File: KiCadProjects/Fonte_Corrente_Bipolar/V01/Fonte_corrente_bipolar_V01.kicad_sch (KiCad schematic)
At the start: 48 parts, among them J1 alimentacao analogica, J2 sinais analogicos, J3 comunicacao / sinais digitais, J4 signal select 1, J5 signal select 2, J7 Vref, U1 INA128, U1-howland1 AD828AN, U2 INA128, U3-cond1 AD828AN

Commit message: Baseado barramento v04 - Finalizado
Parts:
- J4: value signal select 1 -> SinA | Sin1
- J5: value signal select 2 -> SinB | Sin2
- J7: value Vref -> +3.3V | +5.0V
- renumbered D5 to L1:+9v1, D6 to L2:-9v1, D7 to L3:+5v1, D8 to L4:+3.3v1, RganhoINA1 to Rganho-I1, RganhoINA2 to Rganho-I2, Rsentinela1 to Rsentinela-I1, Rsentinela2 to Rsentinela-I2, U2 to U1-INA-I1, U1 to U2-INA-I2
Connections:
- net nó1: now also C3.2; no longer C3.1
- net nó2: now also C3.1; no longer C3.2
- net nó3: now also C1.2; no longer C1.1
- net nó4: now also C1.1; no longer C1.2
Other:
- moved on the sheet: C1, C3
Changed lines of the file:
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@@
   (symbol (lib_id "Device:LED") (at 47.625 120.269 90) (unit 1)
     (in_bom yes) (on_board yes) (dnp no) (fields_autoplaced)
-    (property "Reference" "D7" (at 50.8 120.5865 90)
+    (property "Reference" "L3:+5v1" (at 50.8 120.5865 90)
       (effects (font (size 1.27 1.27)) (justify right))
     )
@@
       (project "Fonte_corrente_bipolar_V01"
         (path "/f0ff92cf-26e5-4ab9-977d-5f9689e8a5d0"
-          (reference "D7") (unit 1)
+          (reference "L3:+5v1") (unit 1)
         )
       )
@@
   (symbol (lib_id "Device:R") (at 213.868 64.643 0) (unit 1)
     (in_bom yes) (on_board yes) (dnp no) (fields_autoplaced)
-    (property "Reference" "RganhoINA2" (at 216.408 63.373 0)
-      (effects (font (size 1.27 1.27)) (justify left))
-    )
-    (property "Value" "3,3k" (at 216.408 65.913 0)
+    (property "Reference" "Rganho-I2" (at 215.9 63.373 0)
+      (effects (font (size 1.27 1.27)) (justify left))
+    )
+    (property "Value" "3,3k" (at 215.9 65.913 0)
       (effects (font (size 1.27 1.27)) (justify left))
     )
@@
       (project "Fonte_corrente_bipolar_V01"
         (path "/f0ff92cf-26e5-4ab9-977d-5f9689e8a5d0"
-          (reference "RganhoINA2") (unit 1)
+          (reference "Rganho-I2") (unit 1)
         )
       )
@@
   (symbol (lib_id "Amplifier_Instrumentation:INA128") (at 242.189 36.068 0) (unit 1)
     (in_bom yes) (on_board yes) (dnp no)
-    (property "Reference" "U2" (at 248.793 26.924 0)
+    (property "Reference" "U1-INA-I1" (at 248.793 26.924 0)
       (effects (font (size 1.27 1.27)))
     )
@@
       (project "Fonte_corrente_bipolar_V01"
         (path "/f0ff92cf-26e5-4ab9-977d-5f9689e8a5d0"
-          (reference "U2") (unit 1)
+          (reference "U1-INA-I1") (unit 1)
         )
       )
@@
     )
   )
-  (symbol (lib_id "Device:C_Polarized_Small_US") (at 238.252 131.572 90) (unit 1)
-    (in_bom yes) (on_board yes) (dnp no) (fields_autoplaced)
-    (property "Reference" "C3" (at 237.8202 125.857 90)
-      (effects (font (size 1.27 1.27)))
-    )
-    (property "Value" "1 uF" (at 237.8202 128.397 90)
+  (symbol (lib_id "Device:C_Polarized_Small_US") (at 238.252 131.572 270) (mirror x) (unit 1)
+    (in_bom yes) (on_board yes) (dnp no)
+    (property "Reference" "C3" (at 238.6838 125.857 90)
+      (effects (font (size 1.27 1.27)))
+    )
+    (property "Value" "1 uF" (at 238.6838 128.397 90)
       (effects (font (size 1.27 1.27)))
     )
@@
   (symbol (lib_id "Device:R") (at 226.314 36.068 0) (unit 1)
     (in_bom yes) (on_board yes) (dnp no) (fields_autoplaced)
-    (property "Reference" "RganhoINA1" (at 228.854 34.798 0)
-      (effects (font (size 1.27 1.27)) (justify left))
-    )
-    (property "Value" "3,3k" (at 228.854 37.338 0)
+    (property "Reference" "Rganho-I1" (at 228.6 34.798 0)
+      (effects (font (size 1.27 1.27)) (justify left))
+    )
+    (property "Value" "3,3k" (at 228.6 37.338 0)
       (effects (font (size 1.27 1.27)) (justify left))
     )
@@
       (project "Fonte_corrente_bipolar_V01"
         (path "/f0ff92cf-26e5-4ab9-977d-5f9689e8a5d0"
-          (reference "RganhoINA1") (unit 1)
+          (reference "Rganho-I1") (unit 1)
         )
       )
@@
   (symbol (lib_id "Device:R") (at 214.249 36.068 0) (unit 1)
     (in_bom yes) (on_board yes) (dnp no) (fields_autoplaced)
-    (property "Reference" "Rsentinela1" (at 216.154 34.798 0)
-      (effects (font (size 1.27 1.27)) (justify left))
-    )
-    (property "Value" "10" (at 216.154 37.338 0)
+    (property "Reference" "Rsentinela-I1" (at 217.17 34.798 0)
+      (effects (font (size 1.27 1.27)) (justify left))
+    )
+    (property "Value" "10" (at 217.17 37.338 0)
       (effects (font (size 1.27 1.27)) (justify left))
     )
@@
       (project "Fonte_corrente_bipolar_V01"
         (path "/f0ff92cf-26e5-4ab9-977d-5f9689e8a5d0"
-          (reference "Rsentinela1") (unit 1)
+          (reference "Rsentinela-I1") (unit 1)
         )
       )
@@
       (effects (font (size 1.27 1.27)) (justify left) hide)
     )
-    (property "Value" "signal select 2" (at 153.416 61.087 90)
+    (property "Value" "SinB | Sin2" (at 153.416 61.087 90)
       (effects (font (size 1.27 1.27)) (justify right))
     )
@@
   (symbol (lib_id "Device:LED") (at 33.401 120.269 270) (unit 1)
     (in_bom yes) (on_board yes) (dnp no) (fields_autoplaced)
-    (property "Reference" "D6" (at 35.56 117.4115 90)
+    (property "Reference" "L2:-9v1" (at 35.56 117.4115 90)
       (effects (font (size 1.27 1.27)) (justify left))
     )
@@
       (project "Fonte_corrente_bipolar_V01"
         (path "/f0ff92cf-26e5-4ab9-977d-5f9689e8a5d0"
-          (reference "D6") (unit 1)
+          (reference "L2:-9v1") (unit 1)
         )
       )
@@
       (effects (font (size 1.27 1.27)) (justify left) hide)
     )
-    (property "Value" "Vref" (at 201.676 94.234 90)
+    (property "Value" "+3.3V | +5.0V" (at 196.85 93.98 90)
       (effects (font (size 1.27 1.27)) (justify right))
     )
@@
   (symbol (lib_id "Device:LED") (at 62.103 120.269 90) (unit 1)
     (in_bom yes) (on_board yes) (dnp no) (fields_autoplaced)
-    (property "Reference" "D8" (at 66.04 120.5865 90)
+    (property "Reference" "L4:+3.3v1" (at 66.04 120.5865 90)
       (effects (font (size 1.27 1.27)) (justify right))
     )
@@
       (project "Fonte_corrente_bipolar_V01"
         (path "/f0ff92cf-26e5-4ab9-977d-5f9689e8a5d0"
-          (reference "D8") (unit 1)
+          (reference "L4:+3.3v1") (unit 1)
         )
       )
@@
   (symbol (lib_id "Device:LED") (at 18.161 120.396 90) (unit 1)
     (in_bom yes) (on_board yes) (dnp no) (fields_autoplaced)
-    (property "Reference" "D5" (at 21.59 120.7135 90)
+    (property "Reference" "L1:+9v1" (at 21.59 120.7135 90)
       (effects (font (size 1.27 1.27)) (justify right))
     )
@@
       (project "Fonte_corrente_bipolar_V01"
         (path "/f0ff92cf-26e5-4ab9-977d-5f9689e8a5d0"
-          (reference "D5") (unit 1)
+          (reference "L1:+9v1") (unit 1)
         )
       )
@@
   (symbol (lib_id "Amplifier_Instrumentation:INA128") (at 229.743 64.643 0) (unit 1)
     (in_bom yes) (on_board yes) (dnp no)
-    (property "Reference" "U1" (at 236.347 55.499 0)
+    (property "Reference" "U2-INA-I2" (at 236.347 55.499 0)
       (effects (font (size 1.27 1.27)))
     )
@@
       (project "Fonte_corrente_bipolar_V01"
         (path "/f0ff92cf-26e5-4ab9-977d-5f9689e8a5d0"
-          (reference "U1") (unit 1)
+          (reference "U2-INA-I2") (unit 1)
         )
       )
@@
       (effects (font (size 1.27 1.27)) (justify left) hide)
     )
-    (property "Value" "signal select 1" (at 25.908 69.85 90)
+    (property "Value" "SinA | Sin1" (at 27.94 63.5 90)
       (effects (font (size 1.27 1.27)) (justify right))
     )
@@
   (symbol (lib_id "Device:R") (at 201.803 64.643 0) (unit 1)
     (in_bom yes) (on_board yes) (dnp no) (fields_autoplaced)
-    (property "Reference" "Rsentinela2" (at 203.708 63.373 0)
-      (effects (font (size 1.27 1.27)) (justify left))
-    )
-    (property "Value" "10" (at 203.708 65.913 0)
+    (property "Reference" "Rsentinela-I2" (at 204.47 63.373 0)
+      (effects (font (size 1.27 1.27)) (justify left))
+    )
+    (property "Value" "10" (at 204.47 65.913 0)
       (effects (font (size 1.27 1.27)) (justify left))
     )
@@
       (project "Fonte_corrente_bipolar_V01"
         (path "/f0ff92cf-26e5-4ab9-977d-5f9689e8a5d0"
-          (reference "Rsentinela2") (unit 1)
+          (reference "Rsentinela-I2") (unit 1)
         )
       )
@@
     )
   )
-  (symbol (lib_id "Device:C_Polarized_Small_US") (at 167.259 129.54 270) (mirror x) (unit 1)
-    (in_bom yes) (on_board yes) (dnp no) (fields_autoplaced)
-    (property "Reference" "C1" (at 167.6908 123.825 90)
-      (effects (font (size 1.27 1.27)))
-    )
-    (property "Value" "1 uF" (at 167.6908 126.365 90)
-      (effects (font (size 1.27 1.27)))
-    )
+  (symbol (lib_id "Device:C_Polarized_Small_US") (at 167.259 129.54 90) (unit 1)
+    (in_bom yes) (on_board yes) (dnp no)
+    (property "Reference" "C1" (at 166.8272 123.825 90)
+      (effects (font (size 1.27 1.27)))
+    )
+    (property "Value" "1 uF" (at 166.8272 126.365 90)
+      (effects (font (size 1.27 1.27)))
+    )

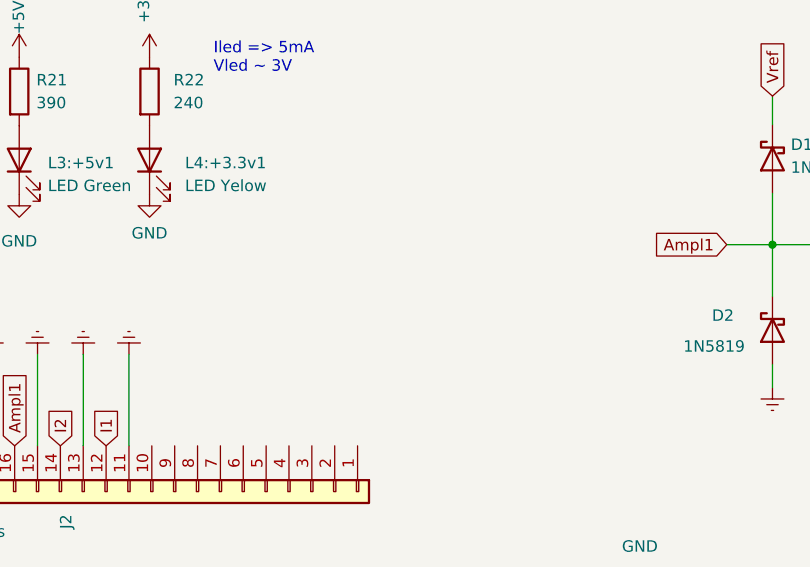
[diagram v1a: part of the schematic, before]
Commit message: Baseado barramento v04 - Finalizado - implementacao resistor pullup i2c 2
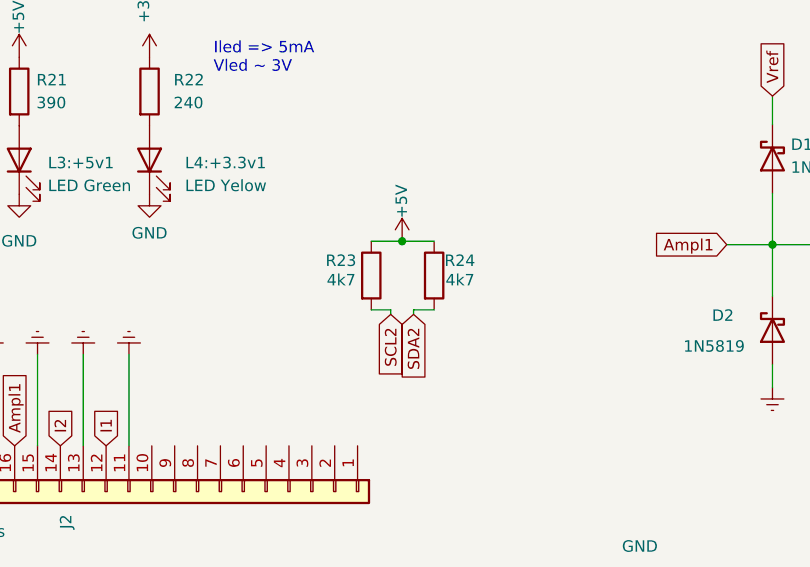
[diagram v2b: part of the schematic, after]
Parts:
- added R23, R24: 4k7, Resistor_THT:R_Axial_DIN0207_L6.3mm_D2.5mm_P7.62mm_Horizontal, symbol Device:R
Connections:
- net +5V: now also R23.1, R24.1
- net SCL2: now also R23.2
- net SDA2: now also R24.2
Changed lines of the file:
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@@
   (junction (at 50.165 40.64) (diameter 0) (color 0 0 0 0)
   )
+  (junction (at 90.17 129.286) (diameter 0) (color 0 0 0 0)
+  )
   (junction (at 120.65 68.58) (diameter 0) (color 0 0 0 0)
   )
@@
     (stroke (width 0) (type default))
   )
+  (wire (pts (xy 91.44 137.414) (xy 91.44 136.906))
+    (stroke (width 0) (type default))
+  )
   (wire (pts (xy 36.5748 177.038) (xy 36.5748 181.864))
     (stroke (width 0) (type default))
@@
     (stroke (width 0) (type default))
   )
+  (wire (pts (xy 93.726 129.286) (xy 90.17 129.286))
+    (stroke (width 0) (type default))
+  )
   (wire (pts (xy 240.792 131.572) (xy 243.332 131.572))
     (stroke (width 0) (type default))
@@
     (stroke (width 0) (type default))
   )
+  (wire (pts (xy 88.9 137.414) (xy 88.9 136.906))
+    (stroke (width 0) (type default))
+  )
   (wire (pts (xy 131.318 129.667) (xy 126.238 129.667))
     (stroke (width 0) (type default))
@@
     (stroke (width 0) (type default))
   )
+  (wire (pts (xy 90.17 129.286) (xy 86.741 129.286))
+    (stroke (width 0) (type default))
+  )
   (wire (pts (xy 25.908 54.737) (xy 22.733 54.737))
     (stroke (width 0) (type default))
@@
     (stroke (width 0) (type default))
   )
+  (wire (pts (xy 88.9 136.906) (xy 86.741 136.906))
+    (stroke (width 0) (type default))
+  )
   (wire (pts (xy 50.165 35.56) (xy 50.165 40.64))
     (stroke (width 0) (type default))
@@
     (stroke (width 0) (type default))
   )
+  (wire (pts (xy 91.44 136.906) (xy 93.726 136.906))
+    (stroke (width 0) (type default))
+  )
   (wire (pts (xy 55.88 86.995) (xy 55.88 83.82))
     (stroke (width 0) (type default))
@@
     )
   )
+  (global_label "SDA2" (shape input) (at 91.44 137.414 270) (fields_autoplaced)
+    (effects (font (size 1.27 1.27)) (justify right))
+    (property "Intersheetrefs" "${INTERSHEET_REFS}" (at 91.44 145.1768 90)
+      (effects (font (size 1.27 1.27)) (justify right) hide)
+    )
+  )
   (global_label "Ampl2" (shape input) (at 274.574 131.699 0) (fields_autoplaced)
     (effects (font (size 1.27 1.27)) (justify left))
@@
     )
   )
+  (global_label "SCL2" (shape input) (at 88.9 137.414 270) (fields_autoplaced)
+    (effects (font (size 1.27 1.27)) (justify right))
+    (property "Intersheetrefs" "${INTERSHEET_REFS}" (at 88.9 145.1163 90)
+      (effects (font (size 1.27 1.27)) (justify right) hide)
+    )
+  )
   (global_label "Vref" (shape input) (at 243.332 115.062 90) (fields_autoplaced)
     (effects (font (size 1.27 1.27)) (justify left))
@@
     )
   )
+  (symbol (lib_id "Device:R") (at 93.726 133.096 0) (unit 1)
+    (in_bom yes) (on_board yes) (dnp no)
+    (property "Reference" "R24" (at 94.869 131.445 0)
+      (effects (font (size 1.27 1.27)) (justify left))
+    )
+    (property "Value" "4k7" (at 94.996 133.604 0)
+      (effects (font (size 1.27 1.27)) (justify left))
+    )
+    (property "Footprint" "Resistor_THT:R_Axial_DIN0207_L6.3mm_D2.5mm_P7.62mm_Horizontal" (at 91.948 133.096 90)
+      (effects (font (size 1.27 1.27)) hide)
+    )
+    (property "Datasheet" "~" (at 93.726 133.096 0)
+      (effects (font (size 1.27 1.27)) hide)
+    )
+    (pin "2")
+    (pin "1")
+    (instances
+      (project "Fonte_corrente_bipolar_V01"
+        (path "/f0ff92cf-26e5-4ab9-977d-5f9689e8a5d0"
+          (reference "R24") (unit 1)
+        )
+      )
+    )
+  )
   (symbol (lib_id "power:Earth") (at 24.257 141.859 180) (unit 1)
     (in_bom yes) (on_board yes) (dnp no) (fields_autoplaced)
@@
     )
   )
+  (symbol (lib_id "Device:R") (at 86.741 133.096 0) (unit 1)
+    (in_bom yes) (on_board yes) (dnp no)
+    (property "Reference" "R23" (at 81.661 131.445 0)
+      (effects (font (size 1.27 1.27)) (justify left))
+    )
+    (property "Value" "4k7" (at 81.788 133.604 0)
+      (effects (font (size 1.27 1.27)) (justify left))
+    )
+    (property "Footprint" "Resistor_THT:R_Axial_DIN0207_L6.3mm_D2.5mm_P7.62mm_Horizontal" (at 84.963 133.096 90)
+      (effects (font (size 1.27 1.27)) hide)
+    )
+    (property "Datasheet" "~" (at 86.741 133.096 0)
+      (effects (font (size 1.27 1.27)) hide)
+    )
+    (pin "1")
+    (pin "2")
+    (instances
+      (project "Fonte_corrente_bipolar_V01"
+        (path "/f0ff92cf-26e5-4ab9-977d-5f9689e8a5d0"
+          (reference "R23") (unit 1)
+        )
+      )
+    )
+  )
   (symbol (lib_id "Device:R") (at 33.401 112.649 0) (unit 1)
     (in_bom yes) (on_board yes) (dnp no) (fields_autoplaced)
@@
         )
       )
+    )
+  )
+  (symbol (lib_id "power:+5V") (at 90.17 129.286 0) (unit 1)
+    (in_bom yes) (on_board yes) (dnp no)
+    (property "Reference" "#PWR061" (at 90.17 133.096 0)
+      (effects (font (size 1.27 1.27)) hide)
+    )
+    (property "Value" "+5V" (at 90.1159 126.7375 90)
+      (effects (font (size 1.27 1.27)) (justify left))
+    )
+    (property "Footprint" "" (at 90.17 129.286 0)
+      (effects (font (size 1.27 1.27)) hide)
+    )
+    (property "Datasheet" "" (at 90.17 129.286 0)
+      (effects (font (size 1.27 1.27)) hide)
+    )
+    (pin "1")
+    (instances
+      (project "Fonte_corrente_bipolar_V01"
+        (path "/f0ff92cf-26e5-4ab9-977d-5f9689e8a5d0"
+          (reference "#PWR061") (unit 1)
+        )
+      )

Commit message: Baseado barramento v04 - Finalizado
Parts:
- renumbered L4:+3.3v1 to L+3.3v1, L3:+5v1 to L+5v1, L1:+9v1 to L+9v1, L2:-9v1 to L-9v1, R23 to RpSCL2, R24 to RpSDA2
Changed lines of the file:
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@@
+    (stroke (width 0) (type default))
+  )
+  (wire (pts (xy 34.29 69.723) (xy 34.29 66.04))
     (stroke (width 0) (type default))
   )
@@
     (stroke (width 0) (type default))
   )
-  (wire (pts (xy 34.29 66.04) (xy 30.226 66.04))
+  (wire (pts (xy 34.29 69.723) (xy 29.845 69.723))
     (stroke (width 0) (type default))
   )
@@
     )
   )
-  (global_label "out_corrente_1" (shape input) (at 30.226 66.04 180) (fields_autoplaced)
+  (global_label "out_corrente_1" (shape input) (at 29.845 69.723 180) (fields_autoplaced)
     (effects (font (size 1.27 1.27)) (justify right))
-    (property "Intersheetrefs" "${INTERSHEET_REFS}" (at 13.2105 66.04 0)
+    (property "Intersheetrefs" "${INTERSHEET_REFS}" (at 12.8295 69.723 0)
       (effects (font (size 1.27 1.27)) (justify right) hide)
     )
@@
   (symbol (lib_id "Device:LED") (at 47.625 120.269 90) (unit 1)
     (in_bom yes) (on_board yes) (dnp no) (fields_autoplaced)
-    (property "Reference" "L3:+5v1" (at 50.8 120.5865 90)
+    (property "Reference" "L+5v1" (at 50.8 120.5865 90)
       (effects (font (size 1.27 1.27)) (justify right))
     )
@@
       (project "Fonte_corrente_bipolar_V01"
         (path "/f0ff92cf-26e5-4ab9-977d-5f9689e8a5d0"
-          (reference "L3:+5v1") (unit 1)
+          (reference "L+5v1") (unit 1)
         )
       )
@@
   (symbol (lib_id "Device:LED") (at 33.401 120.269 270) (unit 1)
     (in_bom yes) (on_board yes) (dnp no) (fields_autoplaced)
-    (property "Reference" "L2:-9v1" (at 35.56 117.4115 90)
+    (property "Reference" "L-9v1" (at 35.56 117.4115 90)
       (effects (font (size 1.27 1.27)) (justify left))
     )
@@
       (project "Fonte_corrente_bipolar_V01"
         (path "/f0ff92cf-26e5-4ab9-977d-5f9689e8a5d0"
-          (reference "L2:-9v1") (unit 1)
+          (reference "L-9v1") (unit 1)
         )
       )
@@
   (symbol (lib_id "Device:R") (at 93.726 133.096 0) (unit 1)
     (in_bom yes) (on_board yes) (dnp no)
-    (property "Reference" "R24" (at 94.869 131.445 0)
+    (property "Reference" "RpSDA2" (at 94.869 131.445 0)
       (effects (font (size 1.27 1.27)) (justify left))
     )
@@
       (project "Fonte_corrente_bipolar_V01"
         (path "/f0ff92cf-26e5-4ab9-977d-5f9689e8a5d0"
-          (reference "R24") (unit 1)
+          (reference "RpSDA2") (unit 1)
         )
       )
@@
   (symbol (lib_id "Device:LED") (at 62.103 120.269 90) (unit 1)
     (in_bom yes) (on_board yes) (dnp no) (fields_autoplaced)
-    (property "Reference" "L4:+3.3v1" (at 66.04 120.5865 90)
+    (property "Reference" "L+3.3v1" (at 66.04 120.5865 90)
       (effects (font (size 1.27 1.27)) (justify right))
     )
@@
       (project "Fonte_corrente_bipolar_V01"
         (path "/f0ff92cf-26e5-4ab9-977d-5f9689e8a5d0"
-          (reference "L4:+3.3v1") (unit 1)
+          (reference "L+3.3v1") (unit 1)
         )
       )
@@
   (symbol (lib_id "Device:LED") (at 18.161 120.396 90) (unit 1)
     (in_bom yes) (on_board yes) (dnp no) (fields_autoplaced)
-    (property "Reference" "L1:+9v1" (at 21.59 120.7135 90)
+    (property "Reference" "L+9v1" (at 21.59 120.7135 90)
       (effects (font (size 1.27 1.27)) (justify right))
     )
@@
       (project "Fonte_corrente_bipolar_V01"
         (path "/f0ff92cf-26e5-4ab9-977d-5f9689e8a5d0"
-          (reference "L1:+9v1") (unit 1)
+          (reference "L+9v1") (unit 1)
         )
       )
@@
       (effects (font (size 1.27 1.27)) (justify left) hide)
     )
-    (property "Value" "SinA | Sin1" (at 27.94 63.5 90)
+    (property "Value" "SinA | Sin1" (at 25.654 64.262 90)
       (effects (font (size 1.27 1.27)) (justify right))
     )
@@
   (symbol (lib_id "Device:R") (at 86.741 133.096 0) (unit 1)
     (in_bom yes) (on_board yes) (dnp no)
-    (property "Reference" "R23" (at 81.661 131.445 0)
+    (property "Reference" "RpSCL2" (at 78.232 131.191 0)
       (effects (font (size 1.27 1.27)) (justify left))
     )
@@
       (project "Fonte_corrente_bipolar_V01"
         (path "/f0ff92cf-26e5-4ab9-977d-5f9689e8a5d0"
-          (reference "R23") (unit 1)
-        )
-      )
+          (reference "RpSCL2") (unit 1)
+        )
+      )

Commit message: temp
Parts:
- added RpSCL1, RpSCL3, RpSCL4, RpSDA1, RpSDA3, RpSDA4: 4k7, Resistor_THT:R_Axial_DIN0207_L6.3mm_D2.5mm_P7.62mm_Horizontal, symbol Device:R
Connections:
- net +3.3V: now also RpSCL2.2, RpSDA2.2, RpSCL1.2, RpSDA1.2
- net +5V: now also RpSCL3.1, RpSCL4.1, RpSDA3.1, RpSDA4.1; no longer RpSCL2.1, RpSDA2.1
- net SCL1: now also RpSCL1.1
- net SCL2: now also RpSCL3.2; no longer RpSCL2.2
- net SCL3: now also RpSCL2.1
- net SCL4: now also RpSCL4.2
- net SDA1: now also RpSDA1.1
- net SDA2: now also RpSDA3.2; no longer RpSDA2.2
- net SDA3: now also RpSDA2.1
- net SDA4: now also RpSDA4.2
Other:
- moved on the sheet: J1, J2, J3, L+3.3v1, L+5v1, L+9v1, L-9v1, R19, R20, R21, R22

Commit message: em producao
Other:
- title: Fonte de corrente monopolar -> Fonte de corrente bipolar
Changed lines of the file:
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@@
   (paper "A4")
   (title_block
-    (title "Fonte de corrente monopolar")
-    (date "2023-07-14")
-    (rev "v02")
+    (title "Fonte de corrente bipolar")
+    (date "2024-06-06")
+    (rev "v01")
     (company "EITduino")
     (comment 1 "Autor: Gustavo Pinheiro")
-    (comment 2 "Placa de face dupla 90x100 mm")
+    (comment 2 "Placa de face dupla 100x100 mm")
     (comment 3 "Barramento V04")
     (comment 4 "Howland aperfeicoada")
